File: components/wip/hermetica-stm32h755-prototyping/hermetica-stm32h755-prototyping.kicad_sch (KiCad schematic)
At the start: 22 parts, among them J128 Conn_01x01, J129 Conn_01x01, J136 Conn_01x01, J137 Conn_01x01, J138 Conn_01x01, J139 Conn_01x01, J140 Conn_01x01, J141 Conn_01x01, J142 Conn_01x01, J143 Conn_01x01, J144 Conn_01x01, J145 Conn_01x01, J146 Conn_01x01, J147 Conn_01x01, J148 Conn_01x01, J149 Conn_01x01, U1 LM66100DCK, U2 LM66100DCK

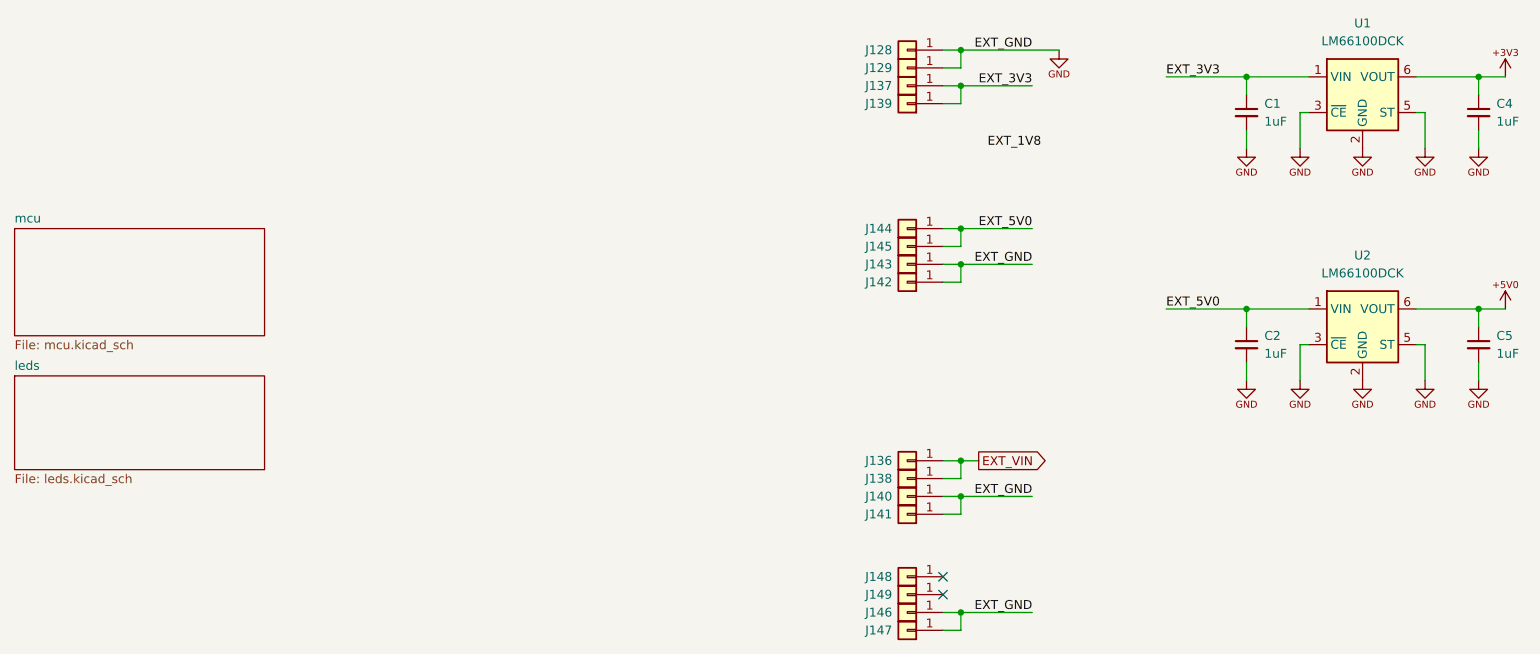
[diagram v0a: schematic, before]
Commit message: STM32H755ZIT6 dev board
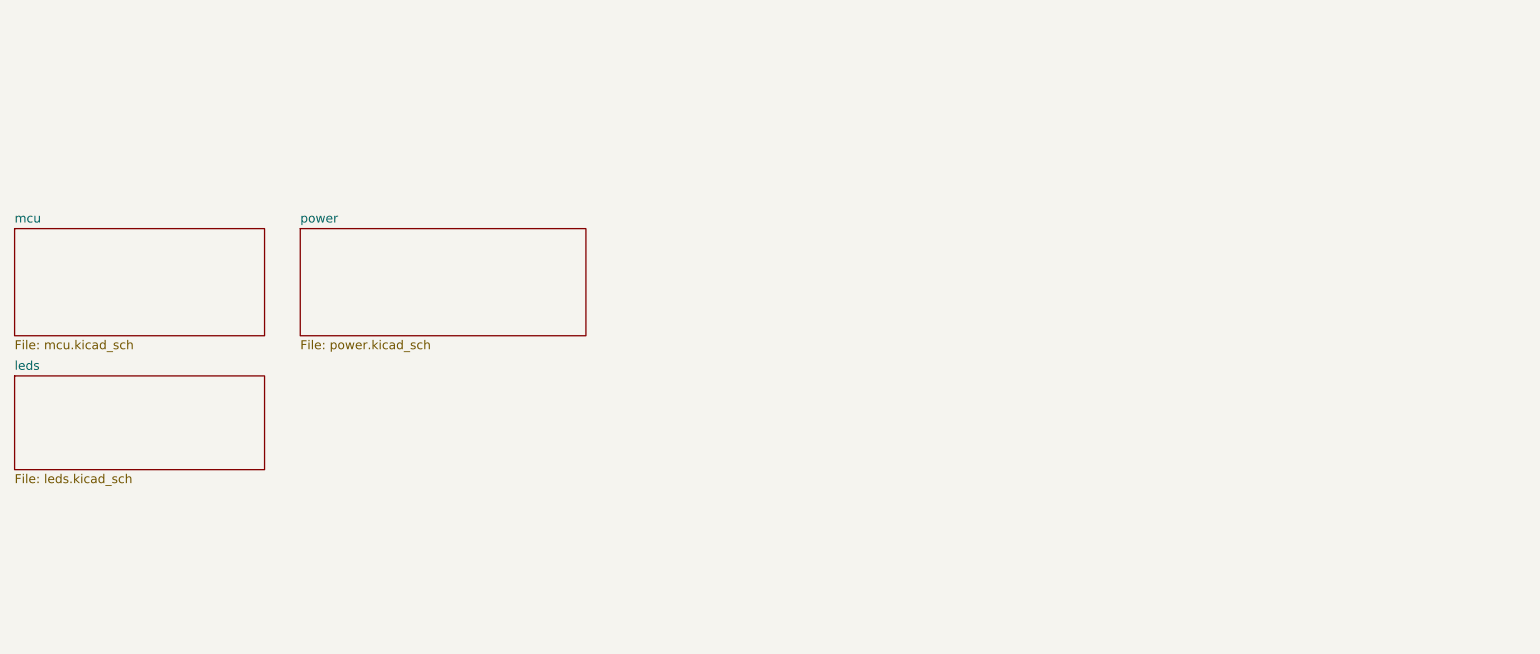
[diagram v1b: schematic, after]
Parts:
- removed C1, C2, C4, C5: 1uF, djStandard:C_0402_1005Metric, symbol DJ:C
- removed J128, J129, J136, J137, J138, J139, J140, J141, J142, J143, J144, J145, J146, J147, J148, J149: Conn_01x01, djStandard:CONNECTOR-PCB-HANDSOLDER-01X01-MALE, symbol Connector_Generic:Conn_01x01
- removed U1, U2: LM66100DCK, Package_TO_SOT_SMD:SOT-363_SC-70-6, symbol Power_Management:LM66100DCK
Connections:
- no-connect marks 2 -> 0
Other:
- added sheet power (power.kicad_sch)
